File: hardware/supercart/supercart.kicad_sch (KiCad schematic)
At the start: 3 parts, among them J1 C64_EDGE_CONNECTOR_44, U1 ATF22V10C_SUPERCART, U2 AM29F080B_SO44

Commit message: Rework SuperCart layout to match a real reference board; add TestBoard
Cross-verified the whole design against hardware/TestBoard/EpyxFastLoad.kicad_pcb,
a real Epyx FastLoad cartridge reproduction that happened to be sitting in the
repo. Its connector footprint matched our c64-wiki-derived pinout on every
single pin, independently confirming it. Adopted several real details from it:

- Connector pads switched from oval (EasyFlash-derived) to rectangular
  1.5x9mm, matching EpyxFastLoad exactly
- Pins 3 and A tied to +5V/GND (were unconnected) per its real precedent
- Board outline traced exactly from its Edge.Cuts geometry: sharp top
  corners, two inward side notches, 45-degree chamfered connector corners
  (an earlier guess at "rounded corners" from a mirrored screenshot was wrong)
- Board width matched to its 58.0mm; height tightened to 60mm (its 37.9mm
  isn't physically reachable -- our AM29F080B body alone is 28.2mm, verified
  from its datasheet, vs. the small DIP EPROM that board actually uses)

Also: diagnosed and fixed a KiCad DRC false-positive (rotated roundrect SMD
pads triggered bogus adjacent-pin shorts -- fixed by keeping ICs unrotated),
added missing decoupling caps (C1/C2), fixed a placement bug where U2 wasn't
actually top-aligned with U1, and substituted a 3D model for the AM29F080B
footprint since KiCad's own library ships its 2D pads but no matching .step
file.

Co-Authored-By: Claude Sonnet 5 <noreply@anthropic.com>
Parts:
- added C1, C2: 0.1uF, Capacitor_SMD:C_0805_2012Metric, symbol Device:C
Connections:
- net GND: now also J1.A (GND), C1.2, C2.2
- net VCC: now also J1.3 (VCC), C1.1, C2.1
- no-connect marks 18 -> 16

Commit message: Fix U2/J1 KiCad footprint bugs, verify all pinouts, add PINOUTS reference
U2 (AM29F080B): the "horizontal" footprint used a coordinate transpose
instead of a true 90deg rotation, which mirrors (reverses winding of)
the pad layout rather than rotating it -- every pin ended up on the
wrong physical pad. Fixed in make_u2_horizontal_footprint.py, proven
with a shoelace-formula winding check.

J1 (C64 edge connector): numbered (1-22) and lettered (A-Z) pins had
their F.Cu/B.Cu copper-layer assignment backwards relative to a real,
verified reference cartridge (TestBoard/EpyxFastLoad.kicad_pcb). Fixed
in gen_footprints.py; not yet re-applied to the live routed PCB (would
require re-routing J1's traces -- see PINOUTS.md's "Known gap").

Added hardware/supercart/PINOUTS.md and PINOUTS.html: a consolidated,
cited pin map for U1 (ATF22V10C, verified against SUPER_CART_R01.PLD
and its own datasheet, now bundled locally), U2 (AM29F080B, ordering
code decoded as SO-44 not PSOP), and J1, plus the real bank-register/
write-arm logic and static-8K bank map. Also commits the EEPLD PLD
source, exported Gerbers, and the KiCad routing-pipeline scripts
(export_dsn/import_ses/unroute_all/fix_reference_positions) that
weren't in git yet.

Co-Authored-By: Claude Sonnet 5 <noreply@anthropic.com>
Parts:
- removed C2: 0.1uF, Capacitor_SMD:C_0805_2012Metric, symbol Device:C
- added R1: 10k, Resistor_SMD:R_0805_2012Metric, symbol Device:R
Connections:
- net TBD_EXROM_N is gone; now on net GND: J1.9 (EXROM_N)
- net TBD_FLASH_CE_N is gone; now on net FLASH_WE_N: U2.43 (CE_N)
- net TBD_FLASH_OE_N is gone; now on net FLASH_OE_N: U2.29 (OE_N)
- net TBD_FLASH_WE_N is gone; now on net FLASH_WE_N: U2.30 (WE_N)
- net TBD_GAME_N is gone; now on net VCC: J1.8 (GAME_N)
- net TBD_ROML_N is gone; now on net FLASH_WE_N: J1.11 (ROML_N)
- net VCC: now also R1.1
- net TBD_CTRL0 renamed FLASH_OE_N
- net TBD_CTRL1_FLASH_WRITE_SAFETY renamed FLASH_WE_N
- net TBD_CTRL2: no longer names the net of U1.23 (CTRL2)
- no-connect marks 16 -> 17

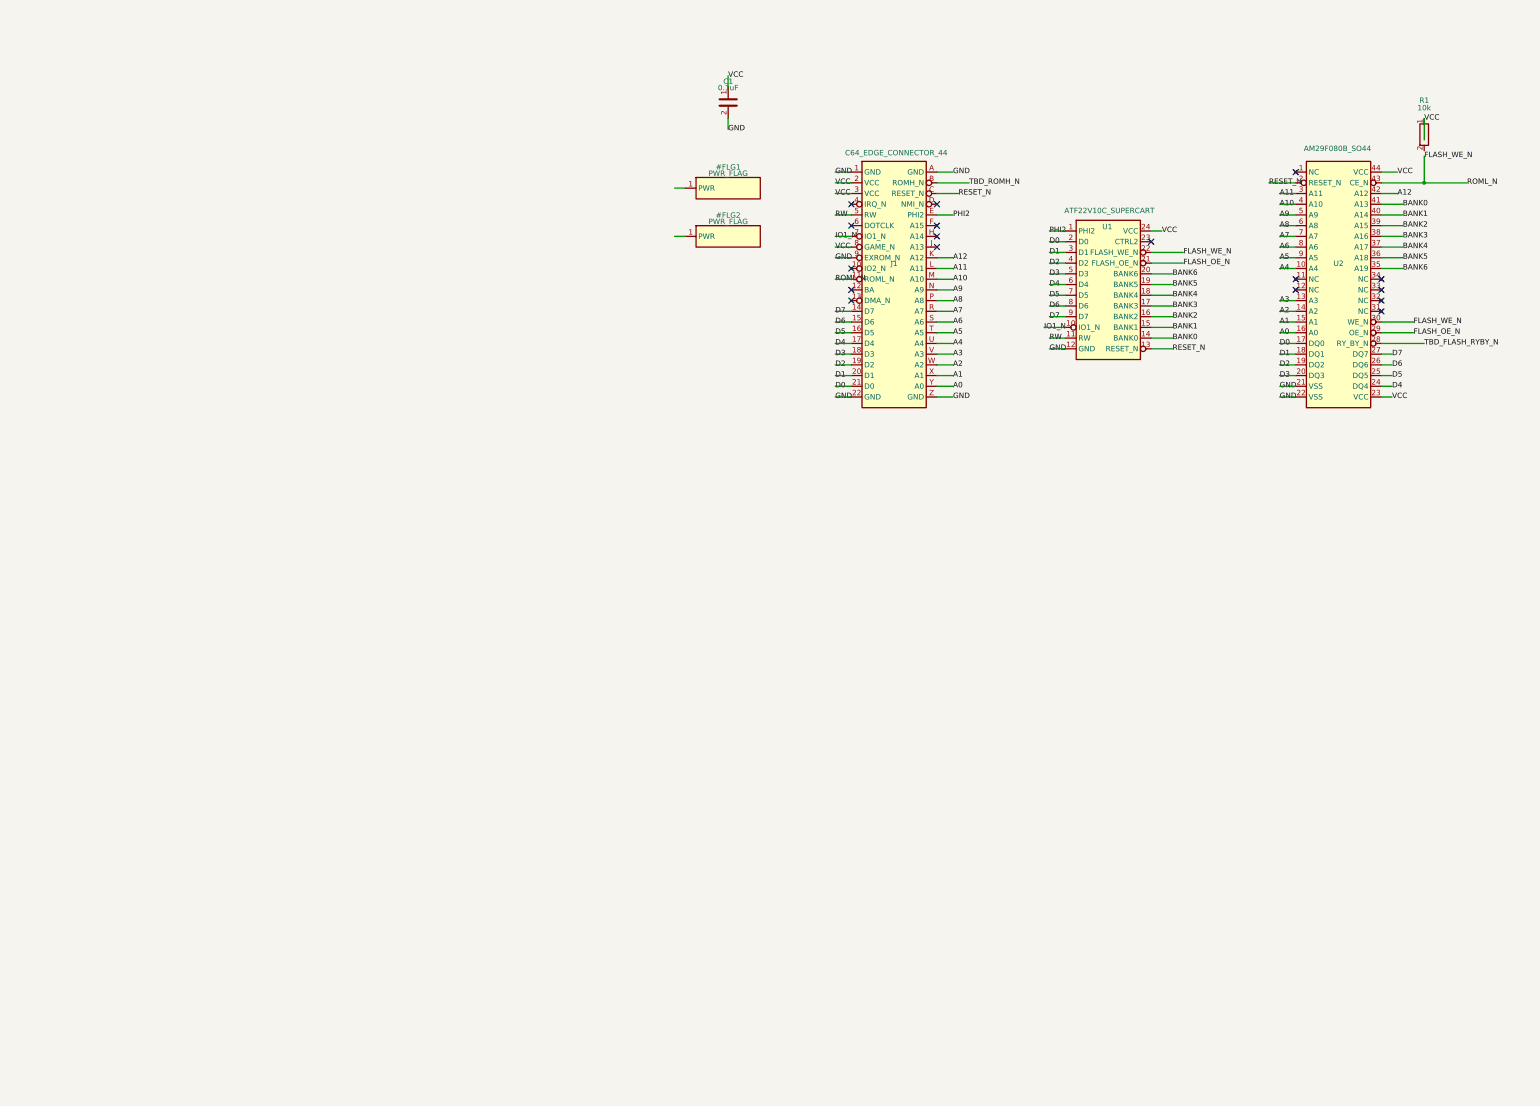
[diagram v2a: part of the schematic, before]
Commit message: Add PWR/WRITE/BUSY status LEDs and real 3D chip-marking text
Status LEDs (schematic + PCB): WRITE taps FLASH_WE_N, BUSY taps U2 pin 28
(RY/BY#) -- both real signals, both active-low, both buffered through
2N7002 MOSFETs wired as shunts across each LED (gate=0 lets a fixed
VCC->R->LED->GND path light it; gate=1 shorts it dark) rather than a
naive series switch, which would light the LED when idle instead of
when active -- verified against the truth table before wiring. RY/BY#
needed a new pull-up (R2): it's a real open-drain output per the
datasheet, previously unused and unpulled. PWR is a plain always-on
indicator. All current-limit resistors are 2.2k per spec; gate resistors
are 100R. Applied to the live schematic via load-and-append (preserves
GUI-edited state) rather than full regeneration.

3D IC body/marking (gen_pcb.py, scripts/make_ic_body_with_marking.py):
custom VRML bodies for U1/U2 with real laser-marking-style text raised
above the surface. Neither KiCad's 2D footprint text nor the VRML `Text`
node actually renders onto a 3D model's surface (both verified directly,
not assumed) -- real marking text requires actual mesh geometry, built
here by reusing the ShackMate logo's potrace/shapely/earcut pipeline in
3D instead of flat silkscreen. U2 also gets a real size fix: it was
previously a PSOP-44 substitute non-uniformly stretched to fit (no real
SO-44 3D model exists anywhere in KiCad's library), which visibly
distorted its corners/bevel; now an exact, undistorted 13.3x28.2mm body.
U1 trades its real, accurately-modeled stock SOIC body for a plainer
custom one to get the marking -- a real visual-fidelity tradeoff made
with explicit sign-off. Corrected "AM29F080B-90PD" (not a real ordering
code for this part -- only E=TSOP or S=SO exist) to the real "-90S".

Also: fix_reference_positions.py extended to hide reference-designator
silkscreen on the new small parts plus LOGO1 and J1 (packing 9 parts
into one 58x15mm strip made individual repositioning fragile; 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
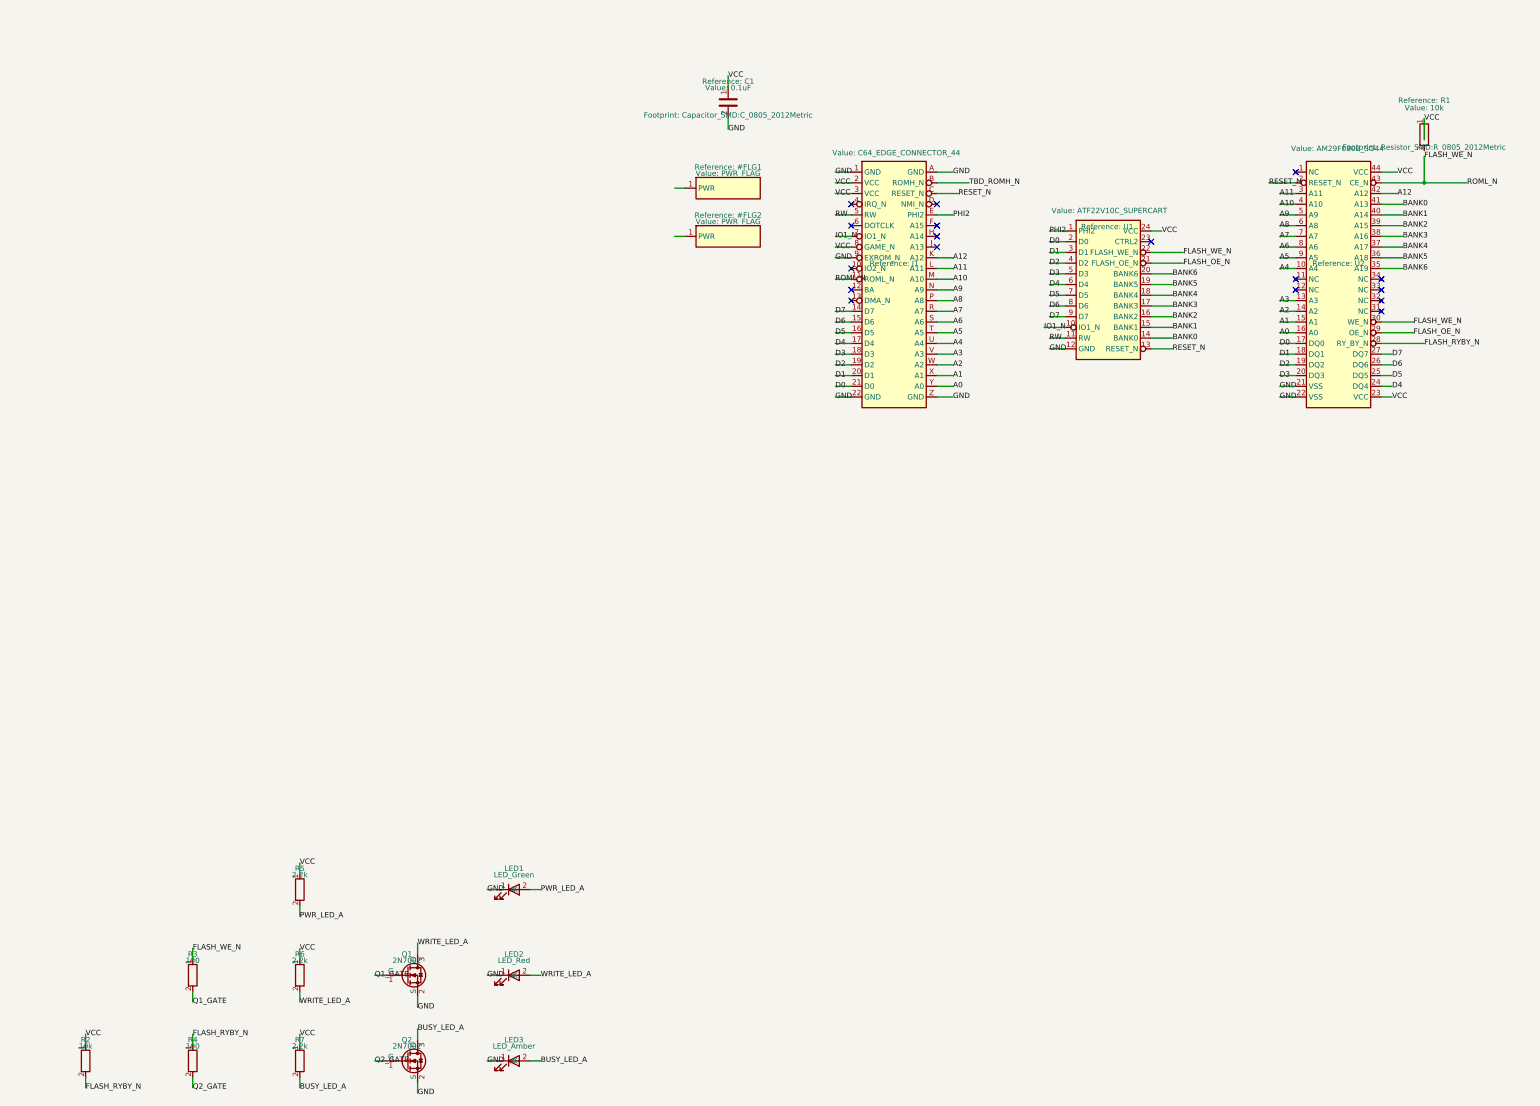
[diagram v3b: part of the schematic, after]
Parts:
- added LED1: LED_Green, LED_SMD:LED_0805_2012Metric, symbol Device:LED
- added LED2: LED_Red, LED_SMD:LED_0805_2012Metric, symbol Device:LED
- added LED3: LED_Amber, LED_SMD:LED_0805_2012Metric, symbol Device:LED
- added Q1, Q2: 2N7002, Package_TO_SOT_SMD:SOT-23, symbol Transistor_FET:Q_NMOS_GSD
- added R2: 10k, Resistor_SMD:R_0805_2012Metric, symbol Device:R
- added R3, R4: 100, Resistor_SMD:R_0805_2012Metric, symbol Device:R
- added R5, R6, R7: 2.2k, Resistor_SMD:R_0805_2012Metric, symbol Device:R
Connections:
- net FLASH_WE_N: now also R3.1
- net GND: now also LED1.1 (K), LED2.1 (K), LED3.1 (K), Q1.2 (S), Q2.2 (S)
- net VCC: now also R2.1, R5.1, R6.1, R7.1
- net TBD_FLASH_RYBY_N renamed FLASH_RYBY_N
- net FLASH_RYBY_N: now also R2.2, R4.1
- new net BUSY_LED_A: LED3.2 (A), Q2.3 (D), R7.2
- new net PWR_LED_A: LED1.2 (A), R5.2
- new net Q1_GATE: Q1.1 (G), R3.2
- new net Q2_GATE: Q2.1 (G), R4.2
- new net WRITE_LED_A: LED2.2 (A), Q1.3 (D), R6.2
